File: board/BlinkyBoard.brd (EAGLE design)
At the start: 33 x 12.2 mm, 18 parts, among them Q1 16 MHz

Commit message: Hopefully Rev A!!
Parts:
- C1: value 0.1uF -> .1uF
- moved U$5 0.25 mm to (18.9, 11.5)
- moved C3 0.25 mm to (27.5, 5.70)
- moved R1 0.25 mm to (10.5, 7.87)
- moved R2 0.25 mm to (10.5, 6.21)
- moved U$3 0.25 mm to (30.8, 6.35)
- moved C2 0.25 mm to (27.5, 2.21)
- moved C7 0.25 mm to (15.8, 1.25)
- moved C8 0.25 mm to (10.5, 1.25)
- moved Q1 0.25 mm to (24.6, 3.85)
- moved C1 0.25 mm to (14.0, 11.3)
- moved C4 0.25 mm to (10.5, 11.3)
- moved C6 0.25 mm to (22.5, 11.3)
- moved S1 0.25 mm to (25.5, 9.00)
- moved U$1 0.25 mm to (17.8, 6.45)
- moved U$2 0.25 mm to (4.00, 6.45)
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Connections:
- net N$3 renamed D-
- net N$4 renamed D+
- net GND: now also U$3.GND; no longer U$3.4
- net MOSI: now also U$3.DATA; no longer U$3.3
- net N$1: now also U$1.38; no longer U$1.41
- net SCK: now also U$3.CLK; no longer U$3.2
- net VCC: now also U$3.+5V; no longer U$3.1
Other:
- board size 33 x 12.2 mm -> 33 x 12.7 mm

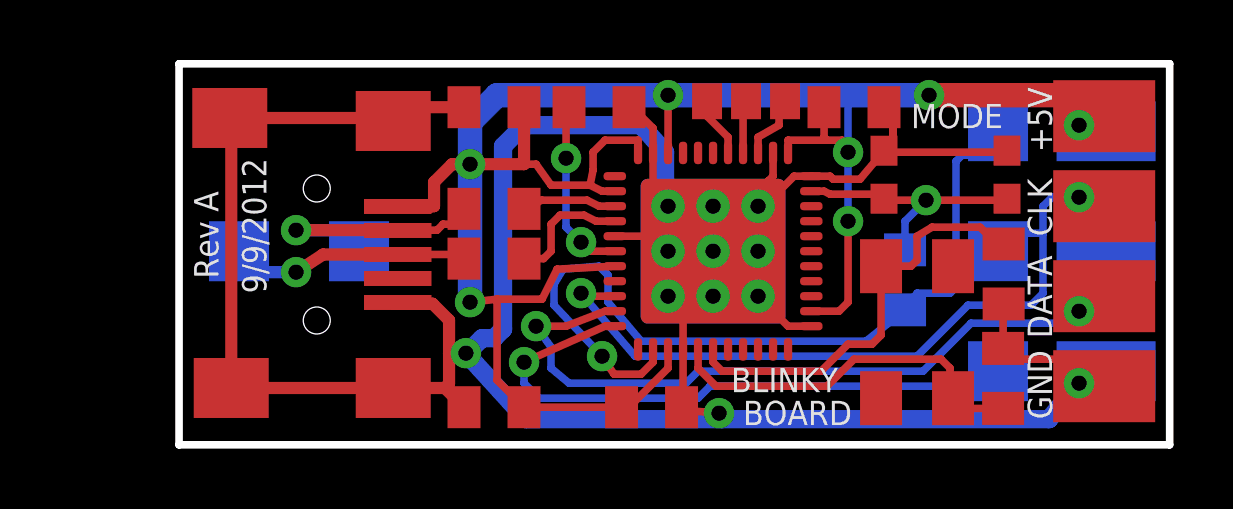
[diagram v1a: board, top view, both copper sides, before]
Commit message: Replace mini USB footprint with Micro USB, swap in 0603 components and smaller crystal, add ground plane to backside
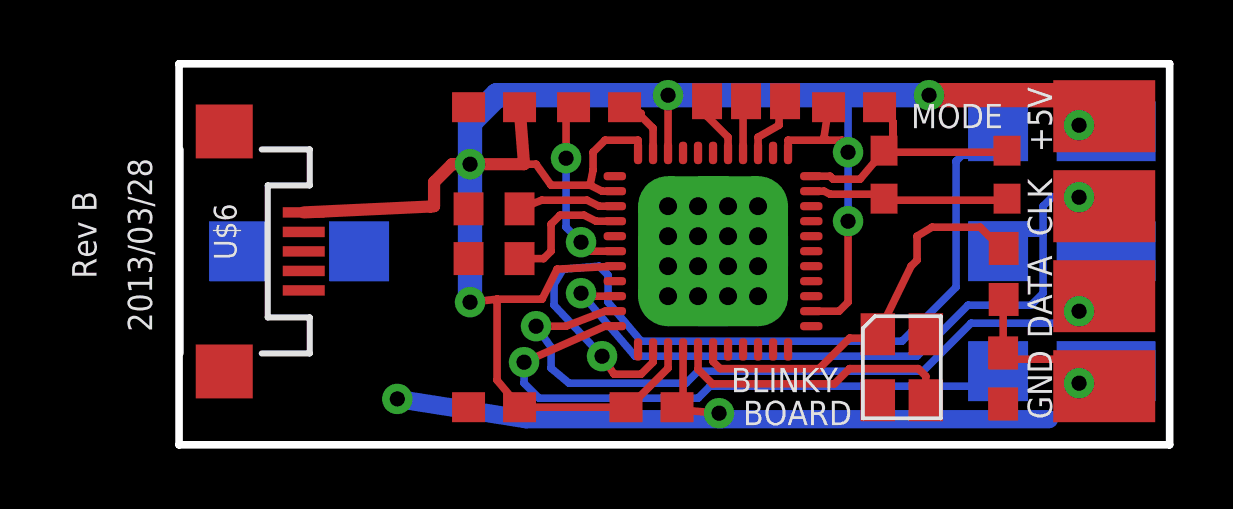
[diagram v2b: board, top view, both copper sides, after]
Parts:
- removed C5: 0uF (DNC), adafruit:C0805K
- C1: value .1uF -> 1uF; device adafruit:C0805K -> adafruit:C0603
- C2, C3, C4, C6, C7, C8: device adafruit:C0805K -> adafruit:C0603
- Q1: device glowboard:ABMM2_CRYSTAL -> blinkiverse:XS3225
- R1, R2: device blinkyboard:ADAFRUIT_R0805 -> adafruit:R0603
- U$1: device blinkyboard:ARDUINO_LEONARDO-REV3B_SMARTPRJ_QFN44ML7X7 -> blinkiverse:ARDUINO_LEONARDO-REV3B_SMARTPRJ_QFN44ML7X7
- U$6: value GLOWBOARD_MINI_USB -> USB-MICROB; device blinkyboard:GLOWBOARD_MINI_USB_PADS -> SparkFun:USB-MICROB
- moved U$6 2.84 mm to (1.51, 6.45)
- moved Q1 1.37 mm to (24.1, 2.58)
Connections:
- net D+_IN: now also U$6.D+; no longer U$6.P$3
- net D-_IN: now also U$6.D-; no longer U$6.P$2
- net GND: now also U$1.PAD@1, U$1.PAD@10, U$1.PAD@11, U$1.PAD@12, U$1.PAD@13, U$1.PAD@14, U$1.PAD@15, U$1.PAD@16, U$1.PAD@2, U$1.PAD@3, U$1.PAD@4, U$1.PAD@5, U$1.PAD@6, U$1.PAD@7, U$1.PAD@8, U$1.PAD@9, U$6.GND; no longer U$1.EXP, U$6.P$5, U$6.P$6, U$6.P$7, U$6.P$8, U$6.P$9
- net N$10: no longer C5.2
- net RST: no longer C5.1
- net VCC: now also U$6.VBUS; no longer U$6.P$1
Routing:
- net GND: track 96.2 -> 43.9 mm
- net N$11: track 15.5 -> 0.00 mm
- net D-_IN: track 8.96 -> 0.00 mm, vias 1 -> 0
- net D+_IN: track 8.66 -> 0.40 mm, vias 1 -> 0
- net VCC: track 72.5 -> 75.7 mm
- net N$8: track 12.6 -> 9.58 mm
- net N$10: track 8.81 -> 6.86 mm, vias 1 -> 0
- net N$9: track 14.2 -> 13.3 mm
- added copper zone on layer 16, net GND
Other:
- board text added: "2013/03/28"
- board text added: "Rev B"
